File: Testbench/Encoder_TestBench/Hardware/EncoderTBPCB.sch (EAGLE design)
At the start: 17 parts, among them IC1 7805DT, U1 ATMEGA328P-PU, X1 C-GRID-05-15-91

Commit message: Upload upon Design Review
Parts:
- removed R3: 1MΩ, resistor:R-US_R0603
- C1: value 100nF -> 0.1µF
- C2, C3: value 100nF -> 10µF
- R1: value 220Ω -> 220
- R2: value 200Ω -> 200
- R4: value 850Ω -> 850
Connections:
- net N$10: no longer R3.2
- net N$11: no longer R3.1
- net N$13: now also U1.PD2; no longer U1.PD1
- net N$14: now also U1.PD3; no longer U1.PD2
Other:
- moved on the sheet: C1, C2, C3, C4, C5, D1, G1, IC1, JP1, JP2, Q1, R1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

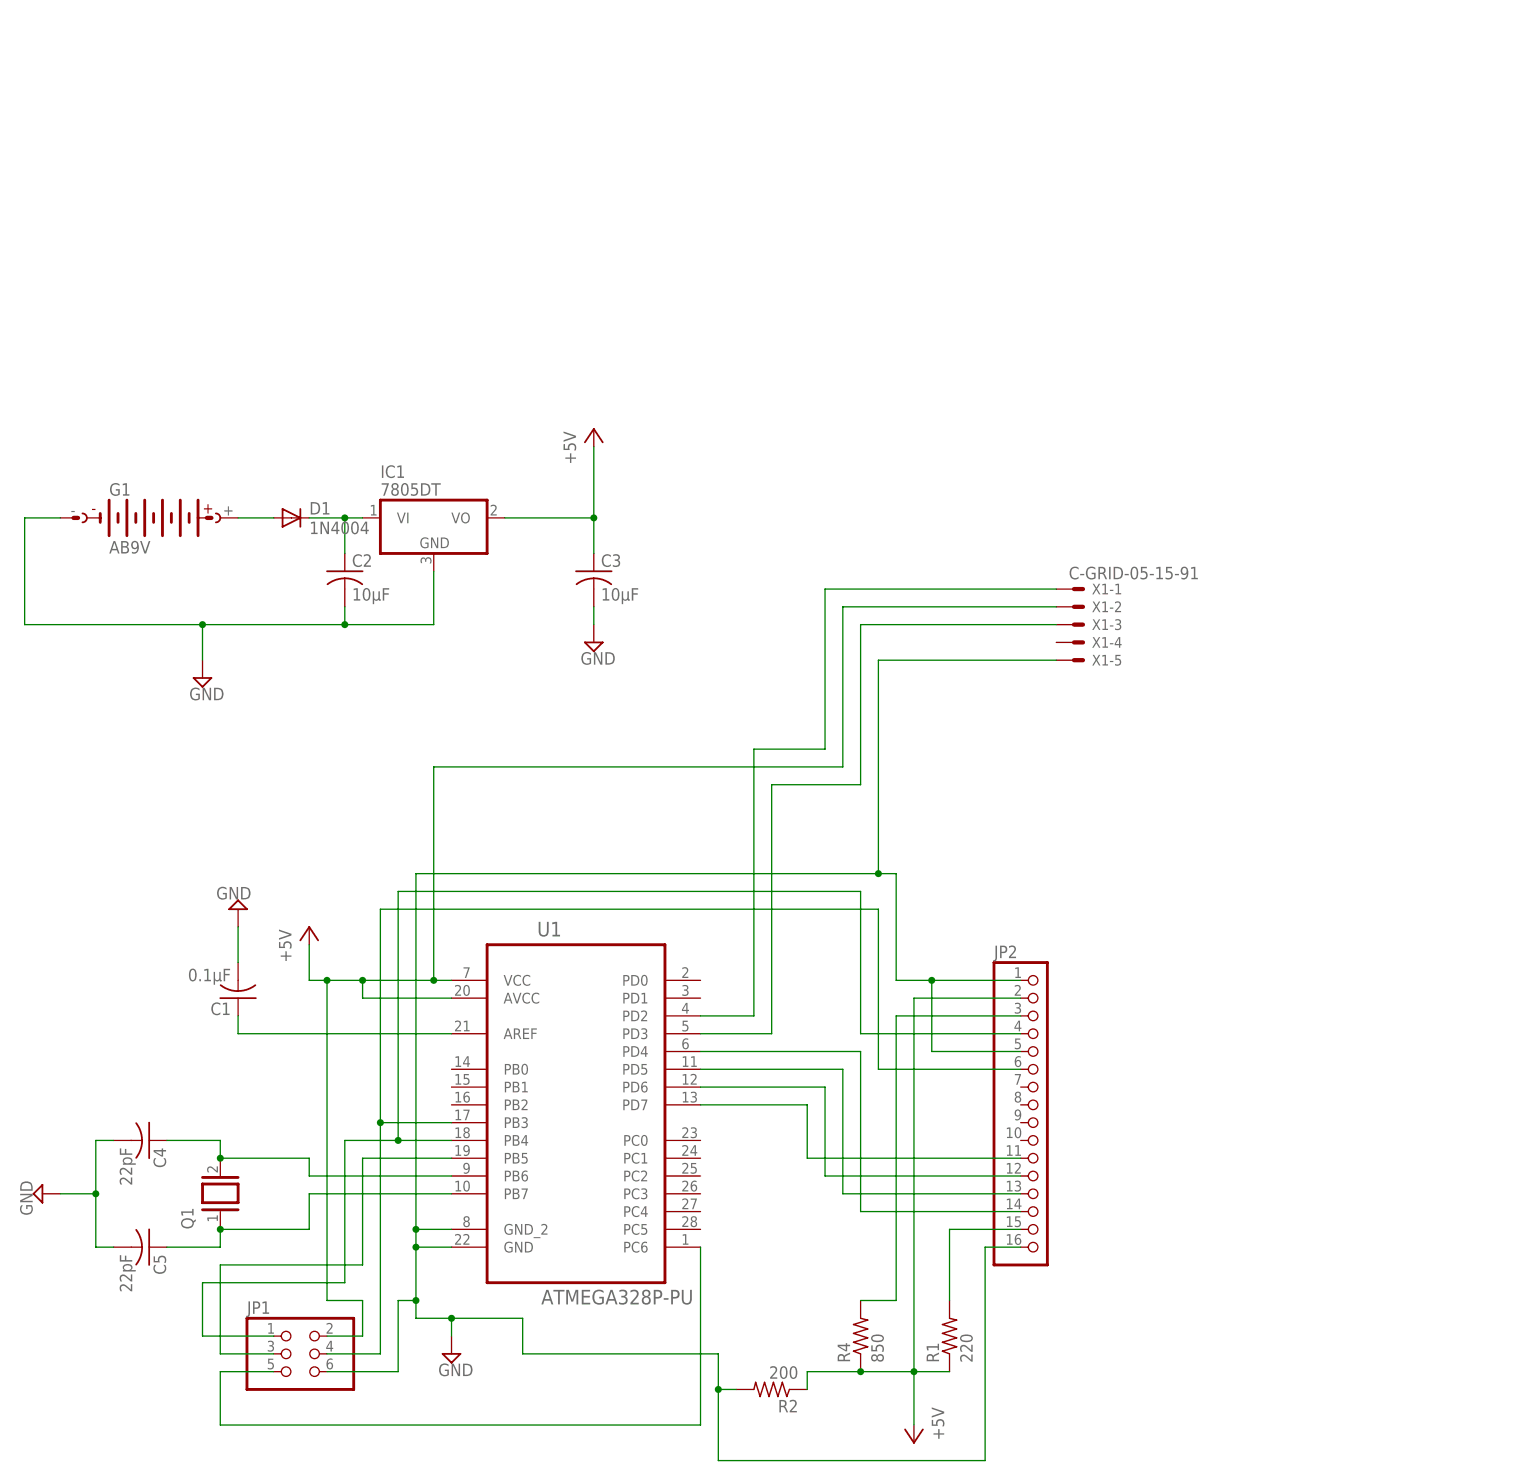
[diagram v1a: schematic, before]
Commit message: Revision Upon Review
Label in lines applied
Capacitors linked to 7805 Regulator value changed according to 7805
data sheet
General Schematics Design Cleanup
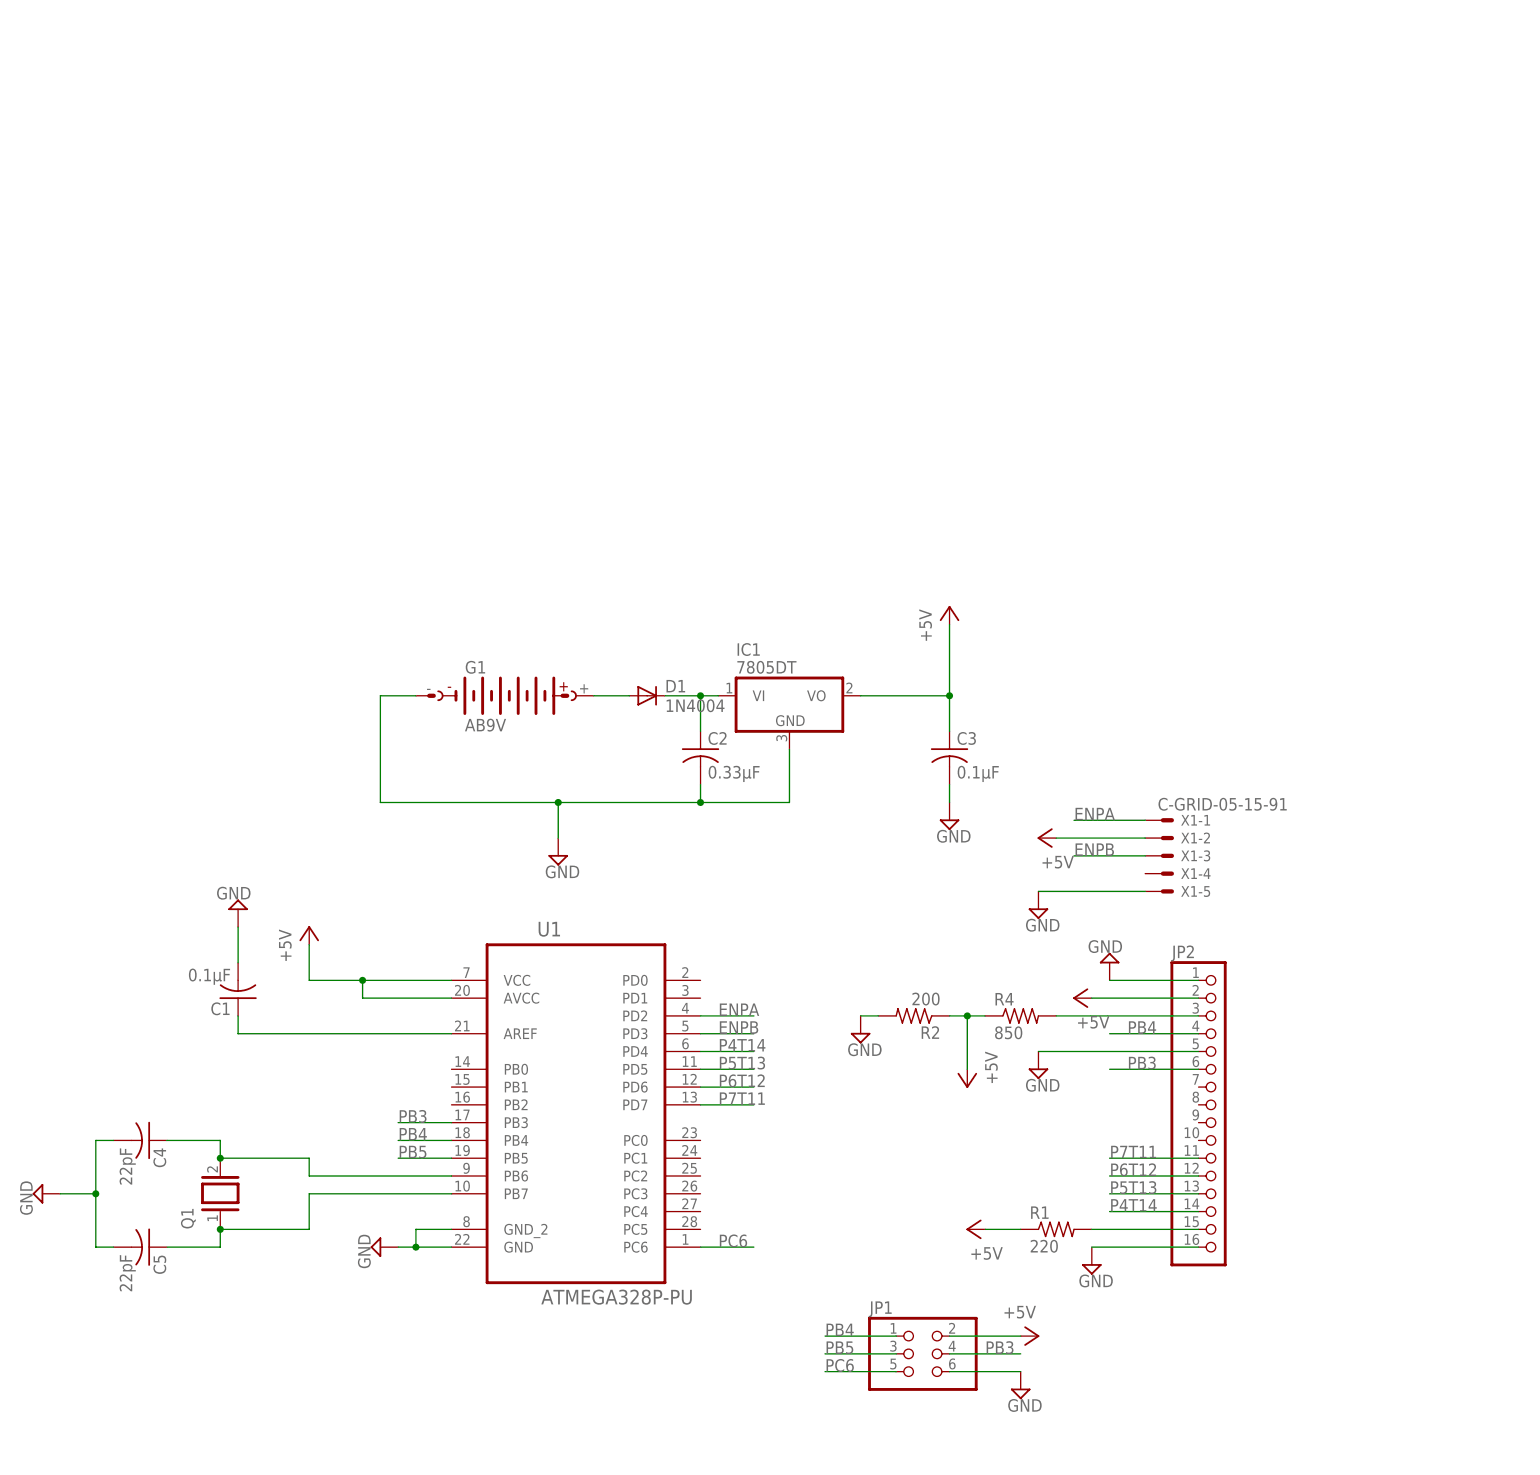
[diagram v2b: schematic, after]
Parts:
- C2: value 10µF -> 0.33µF
- C3: value 10µF -> 0.1µF
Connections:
- net N$1 renamed PB3
- net N$13 renamed ENPA
- net N$14 renamed ENPB
- net N$18 renamed PB5
- net N$19 renamed PC6
- net N$4 renamed P4T14
- net N$5 renamed P5T13
- net N$6 renamed P6T12
- net N$7 renamed P7T11
- net N$9 renamed PB4
- new net +5V: JP1.2, R1.1, R2.1, R4.1, U1.AVCC, U1.VCC, X1-2.S
- new net GND: JP1.6, JP2.1, JP2.16, JP2.5, R2.2, X1-5.S
- net VDD: no longer JP1.2, R1.1, R2.1, R4.1, U1.AVCC, U1.VCC, X1-2.S
- net VSS: no longer JP1.6, JP2.1, JP2.16, JP2.5, R2.2, X1-5.S
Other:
- moved on the sheet: C2, C3, D1, G1, IC1, JP1, JP2, R1, R2, R4, X1-1, X1-2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

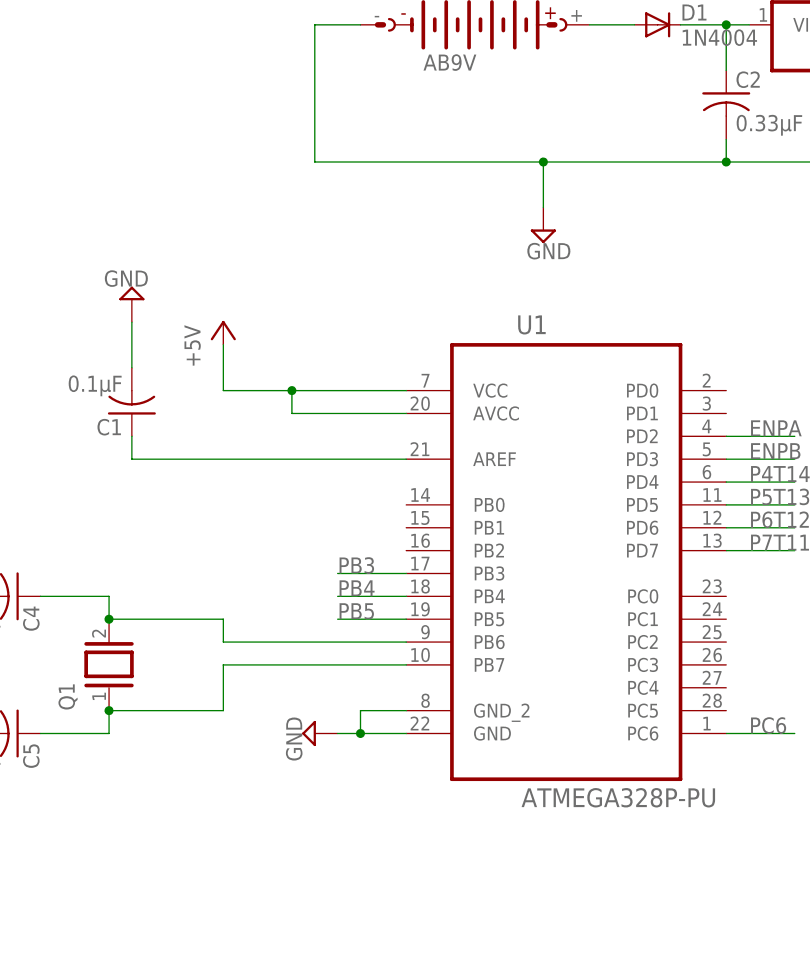
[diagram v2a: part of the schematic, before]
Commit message: Encoder Post-Review Modification
Board Replaced upon comments given by Daniil and Ryo
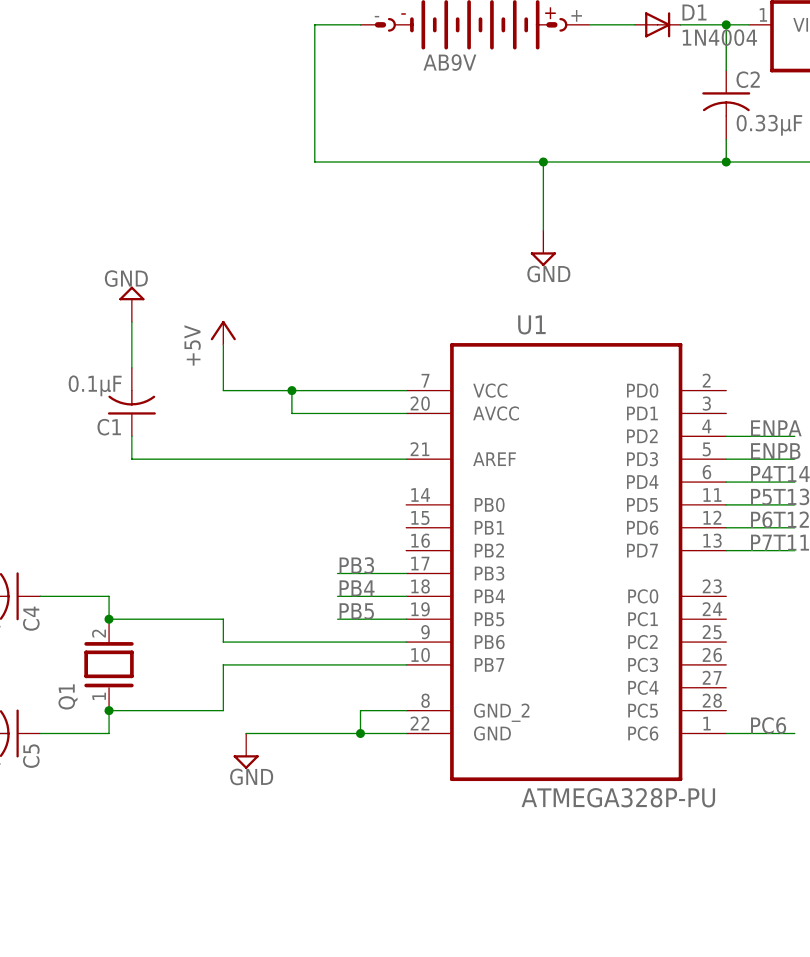
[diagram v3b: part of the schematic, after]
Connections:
- removed net +5V: JP1.2, R1.1, R2.1, R4.1, U1.AVCC, U1.VCC, X1-2.S
- removed net VSS: C1.2, C2.2, C3.2, C4.2, C5.2, G1.-, IC1.GND, U1.GND, U1.GND_2
- net GND: now also C1.2, C2.2, C3.2, C4.2, C5.2, G1.-, IC1.GND, U1.GND, U1.GND_2
- net VDD: now also JP1.2, R1.1, R2.1, R4.1, U1.AVCC, U1.VCC, X1-2.S

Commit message: Testbench Improvement
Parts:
- Q1: value (none) -> 16MHz
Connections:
- net N$10 renamed CRYSTAL
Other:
- note added: "DB"
- note added: "DB1"
- note added: "DB2"
- note added: "DB3"
- note added: "DB4"
- note added: "DB5"
- note added: "DB6"
- note added: "DB7"
- note added: "E"
- note added: "Encoder Pin A"
- note added: "Encoder Pin B"
- note added: "LED+"
- note added: "LED-"
- note added: "R/W"
- note added: "RS"
- note added: "V0"
- note added: "VDD"
- note added: "VSS"
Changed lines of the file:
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@@
 <part name="P+2" library="supply1" deviceset="+5V" device=""/>
 <part name="P+1" library="supply1" deviceset="+5V" device=""/>
-<part name="Q1" library="special" deviceset="XTAL/S" device=""/>
+<part name="Q1" library="special" deviceset="XTAL/S" device="" value="16MHz"/>
 <part name="SUPPLY2" library="supply2" deviceset="GND" device=""/>
 <part name="G1" library="battery" deviceset="AB9V" device=""/>
@@
 <sheet>
 <plain>
+<text x="93.98" y="15.24" size="1.778" layer="91">VSS</text>
+<text x="93.98" y="12.7" size="1.778" layer="91">VDD</text>
+<text x="93.98" y="10.16" size="1.778" layer="91">V0</text>
+<text x="93.98" y="7.62" size="1.778" layer="91">RS</text>
+<text x="93.98" y="5.08" size="1.778" layer="91">R/W</text>
+<text x="93.98" y="2.54" size="1.778" layer="91">E</text>
+<text x="93.98" y="0" size="1.778" layer="91">DB</text>
+<text x="93.98" y="-2.54" size="1.778" layer="91">DB1</text>
+<text x="93.98" y="-5.08" size="1.778" layer="91">DB2</text>
+<text x="93.98" y="-7.62" size="1.778" layer="91">DB3</text>
+<text x="93.98" y="-10.16" size="1.778" layer="91">DB4</text>
+<text x="93.98" y="-12.7" size="1.778" layer="91">DB5</text>
+<text x="93.98" y="-15.24" size="1.778" layer="91">DB6</text>
+<text x="93.98" y="-17.78" size="1.778" layer="91">DB7</text>
+<text x="93.98" y="-20.32" size="1.778" layer="91">LED+</text>
+<text x="93.98" y="-22.86" size="1.778" layer="91">LED-</text>
+<text x="96.52" y="38.1" size="1.778" layer="91">Encoder Pin A</text>
+<text x="96.52" y="33.02" size="1.778" layer="91">Encoder Pin B</text>
 </plain>
 <instances>
@@
 </segment>
 </net>
-<net name="N$10" class="0">
+<net name="CRYSTAL" class="0">
 <segment>
 <wire x1="-17.78" y1="-12.7" x2="-38.1" y2="-12.7" width="0.1524" layer="91"/>

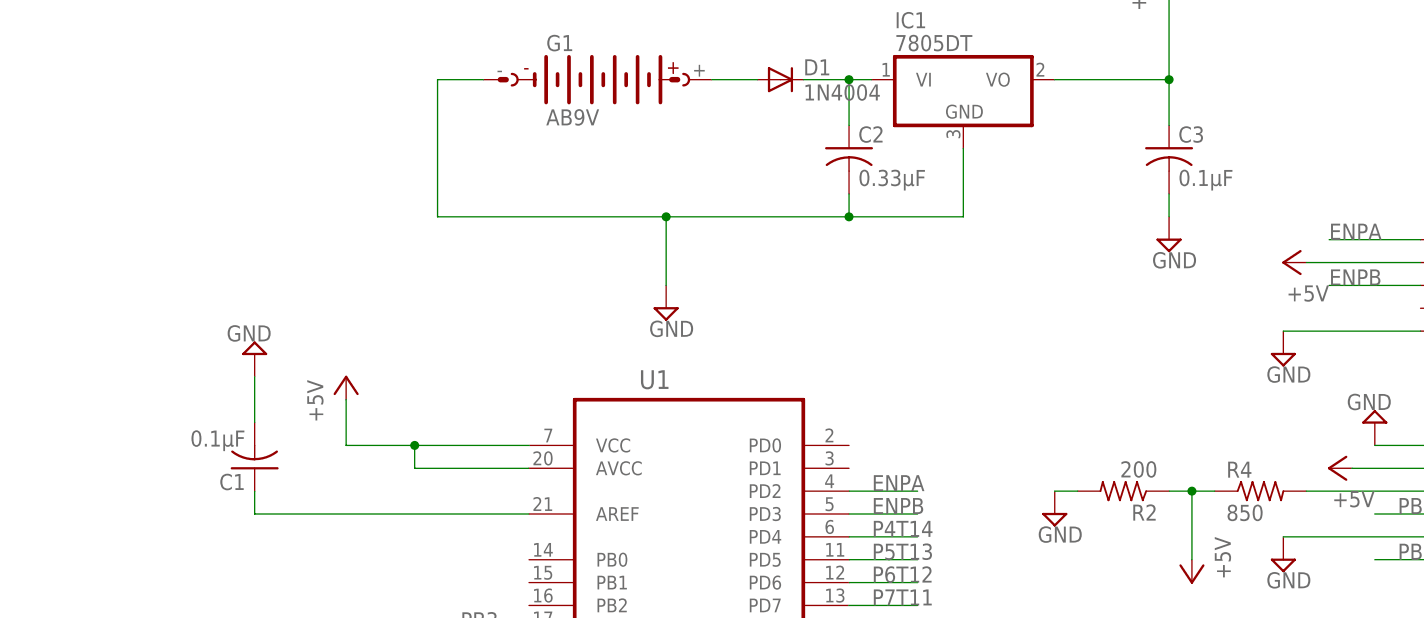
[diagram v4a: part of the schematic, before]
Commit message: Board Design Updated
Updated w/ ground plane
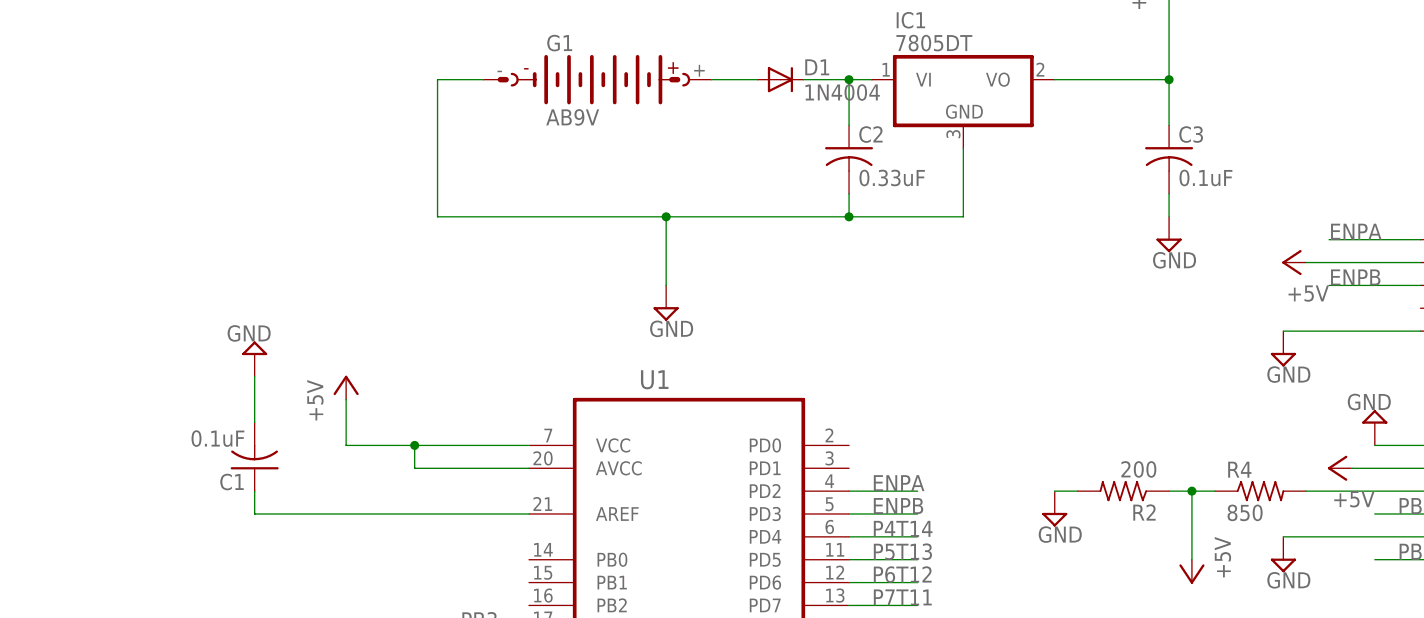
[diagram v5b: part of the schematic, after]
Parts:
- C1, C3: value 0.1µF -> 0.1uF
- C2: value 0.33µF -> 0.33uF
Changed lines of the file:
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@@
 <part name="SUPPLY3" library="supply2" deviceset="GND" device=""/>
 <part name="D1" library="diode" deviceset="1N4004" device=""/>
-<part name="C2" library="resistor" deviceset="C-US" device="C0603" value="0.33µF"/>
-<part name="C3" library="resistor" deviceset="C-US" device="C0603" value="0.1µF"/>
+<part name="C2" library="resistor" deviceset="C-US" device="C0603" value="0.33uF"/>
+<part name="C3" library="resistor" deviceset="C-US" device="C0603" value="0.1uF"/>
 <part name="P+3" library="supply1" deviceset="+5V" device=""/>
 <part name="SUPPLY4" library="supply2" deviceset="GND" device=""/>
@@
 <part name="C4" library="resistor" deviceset="C-US" device="C0603" value="22pF"/>
 <part name="C5" library="resistor" deviceset="C-US" device="C0603" value="22pF"/>
-<part name="C1" library="resistor" deviceset="C-US" device="C0603" value="0.1µF"/>
+<part name="C1" library="resistor" deviceset="C-US" device="C0603" value="0.1uF"/>
 <part name="R4" library="resistor" deviceset="R-US_" device="R0603" value="850"/>
 <part name="R2" library="resistor" deviceset="R-US_" device="R0603" value="200"/>
